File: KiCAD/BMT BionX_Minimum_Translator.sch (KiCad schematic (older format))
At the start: 29 parts

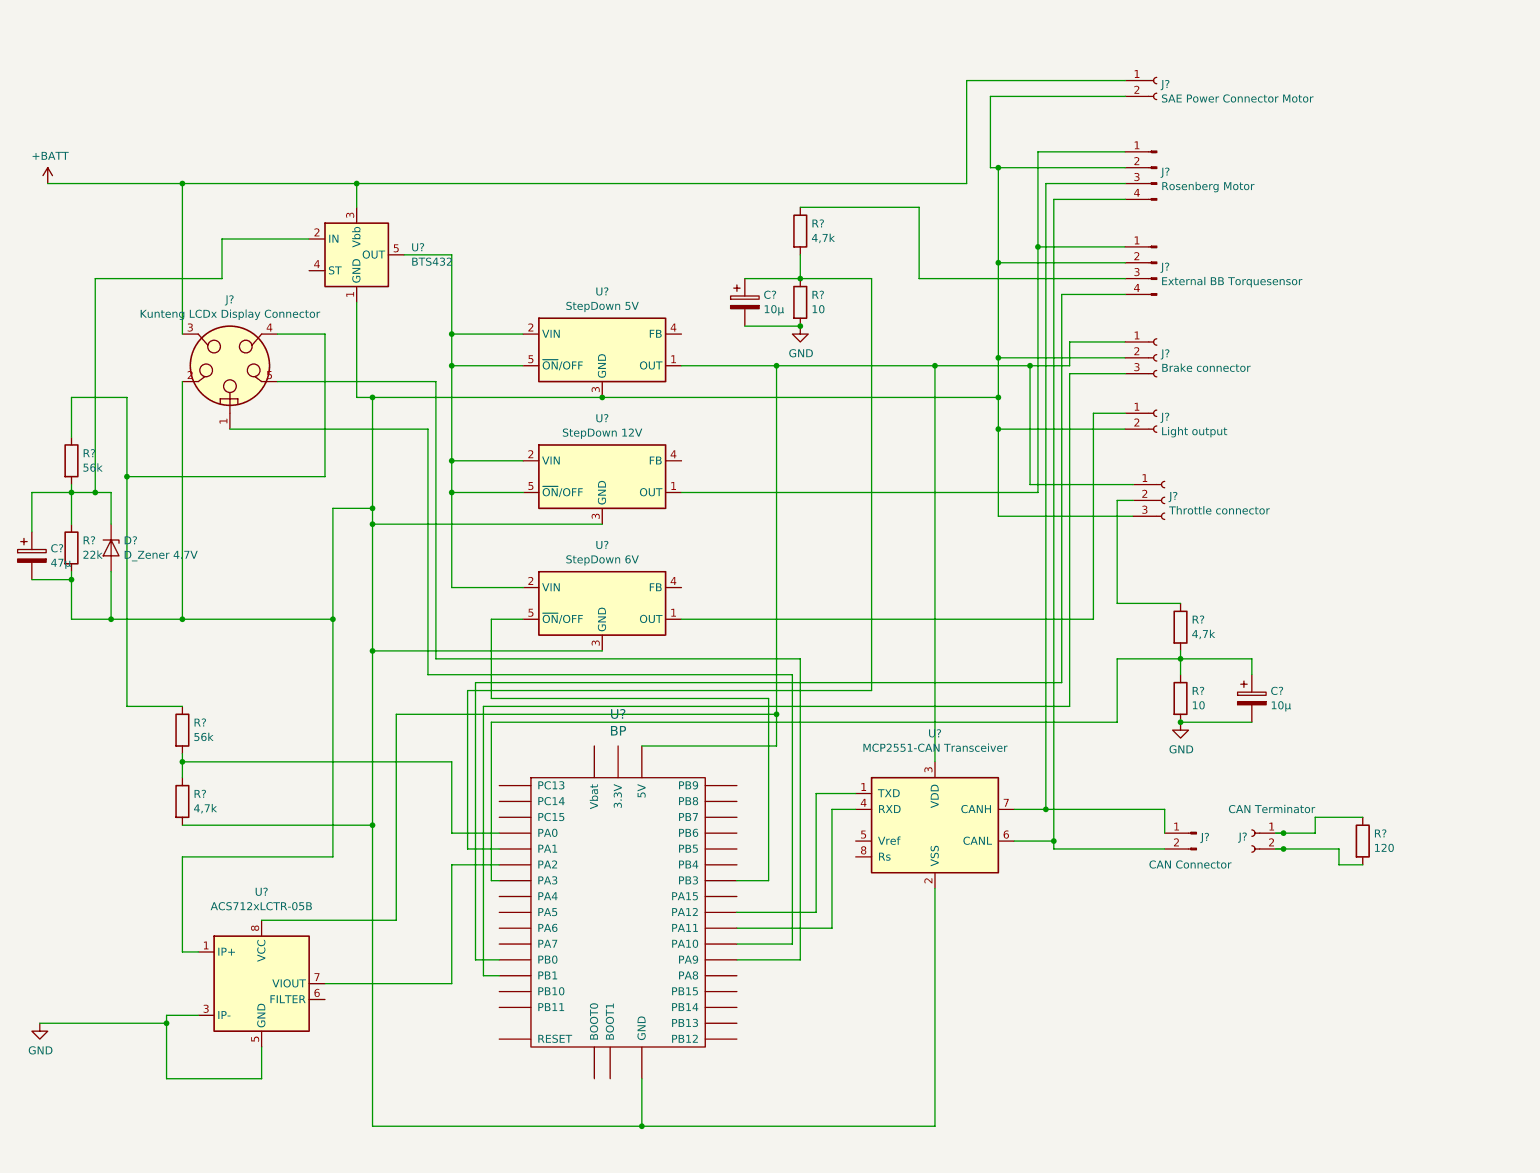
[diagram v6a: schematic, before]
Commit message: Update of schematic with untested "Antiblitz"
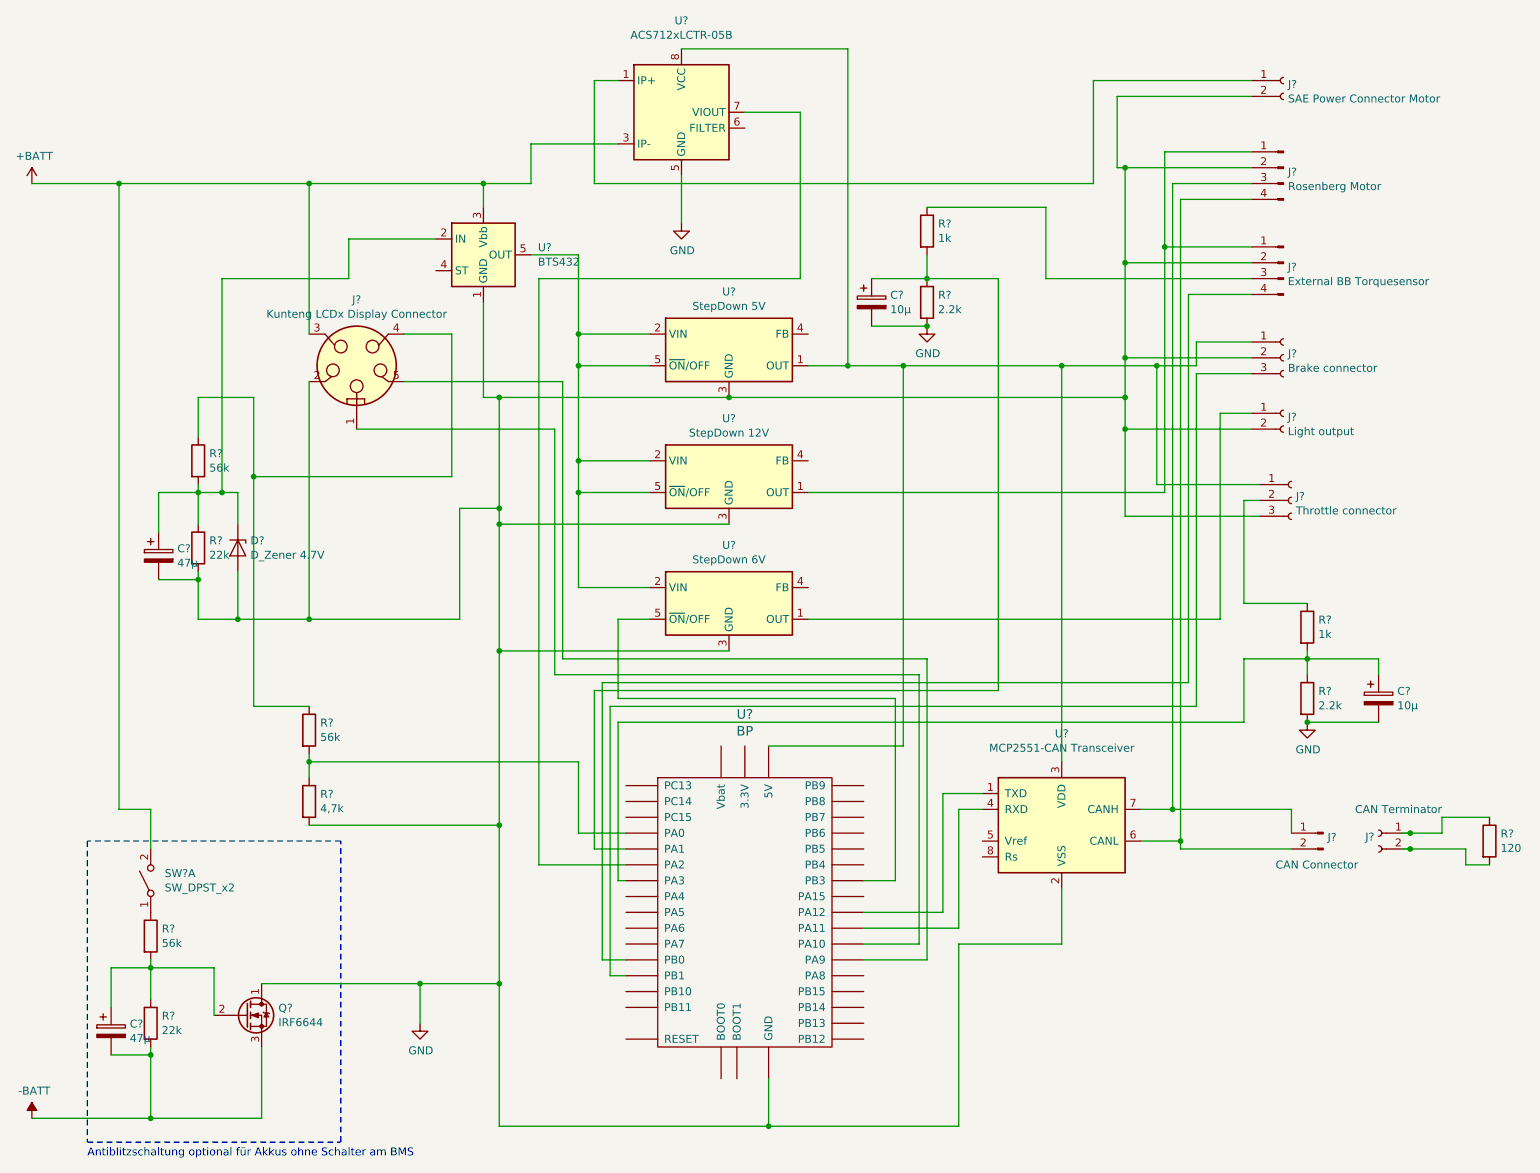
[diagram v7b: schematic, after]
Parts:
- added C?: 47µ, symbol Device:CP
- added Q?: IRF6644, Package_DirectFET:DirectFET_MN, symbol Transistor_FET:IRF6644
- added R?: 56k, symbol Device:R
- added R?: 22k, symbol Device:R
- added SW?: SW_DPST_x2, symbol Switch:SW_DPST_x2
- R? (x2): value 10 -> 2.2k
- R? (x2): value 4,7k -> 1k
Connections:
- net +BATT: now also U?.3 (IP-), U?.4 (IP-), SW?.2 (B); no longer J?.1 (Pin_1)
- net GND: now also C?.2, D?.2 (A), J?.2, J?.2 (Pin_2), J?.2 (Pin_2), J?.2 (Pin_2), J?.2 (Pin_2), J?.2 (Pin_2), J?.3 (Pin_3), R?.2, R?.2, U?.1 (GND), U?.2 (VSS), U?.3 (GND), U?.3 (GND), U?.3 (GND), U?.G (GND), Q?.1 (D); no longer U?.3 (IP-), U?.4 (IP-)
- new net: J?.1 (Pin_1), U?.1 (IP+), U?.2 (IP+)
- new net: C?.1, Q?.2 (G), R?.1, R?.2
- new net: R?.1, SW?.1 (A)
- new net -BATT: C?.2, Q?.3 (S), R?.2
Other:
- note added: "Antiblitzschaltung optional für Akkus ohne Schalter am BMS"
- moved on the sheet: C?, D?, J?, R?, U?
